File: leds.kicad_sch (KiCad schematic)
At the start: 12 parts

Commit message: Improve DCDC converter diagram
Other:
- company: (none) -> Authors: A. Kotkov, I. Kajdan
- title: (none) -> Debug LEDs
- moved on the sheet: D1, D2, D3, R10, R11, R12, R13, R14, R15, R7, R8, R9

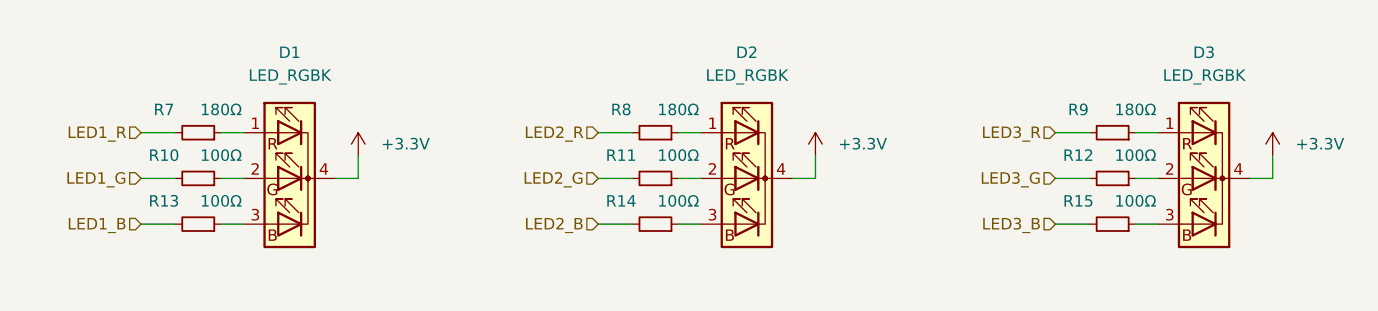
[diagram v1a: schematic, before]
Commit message: Replace RGB leds with single color ones
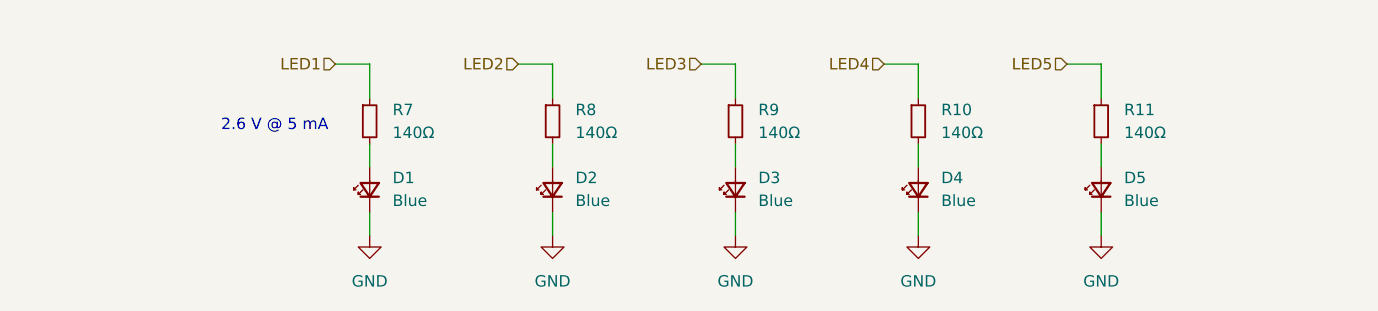
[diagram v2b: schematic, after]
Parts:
- removed D1, D2, D3: LED_RGBK, LED_SMD:LED_Avago_PLCC4_3.2x2.8mm_CW, symbol Device:LED_RGBK
- removed R12, R13, R14, R15: 100Ω, Resistor_SMD:R_0603_1608Metric, symbol Device:R_Small
- added D1, D2, D3, D4, D5: Blue, LED_SMD:LED_0603_1608Metric, symbol Device:LED_Small
- R10, R11: value 100Ω -> 140Ω
- R7, R8, R9: value 180Ω -> 140Ω
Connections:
- net LED3: now reaches R9.1
- net LED5: now reaches R11.1
- net LED2: now reaches R8.1
- net LED1: now reaches R7.1
- net LED4: now reaches R10.1
- net LED1_G: no longer names the net of R10.2
- net LED1_G: now also D4.2 (A)
- net LED1_R: no longer names the net of R7.2
- net LED1_R: now also D1.2 (A)
- net LED2_G: no longer names the net of R11.2
- net LED2_G: now also D5.2 (A)
- net LED2_R: no longer names the net of R8.2
- net LED2_R: now also D2.2 (A)
- net LED3_R: no longer names the net of R9.2
- net LED3_R: now also D3.2 (A)
- new net GND: D1.1 (K), D2.1 (K), D3.1 (K), D4.1 (K), D5.1 (K)
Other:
- note added: "2.6 V @ 5 mA"

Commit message: Use more appropriate MCU pins for peripherals
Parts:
- renumbered D5 to D1, D4 to D2, D2 to D4, D1 to D5, R8 to R10, R7 to R11, R11 to R7, R10 to R8
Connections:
- net LED1: now also R7.1; no longer R11.1
- net LED2: now also R8.1; no longer R10.1
- net LED4: now also R10.1; no longer R8.1
- net LED5: now also R11.1; no longer R7.1
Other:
- moved on the sheet: D1, D2, D4, D5, R10, R11, R7, R8
